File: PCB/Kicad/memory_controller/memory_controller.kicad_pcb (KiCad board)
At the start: 6 copper layers, 180 x 100 mm, 116 parts, among them U1 74245, U10 74283, U11 74377, U12 74377, U13 74245, U14 74245, U15 74245, U16 74245, U17 74245, U18 74245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

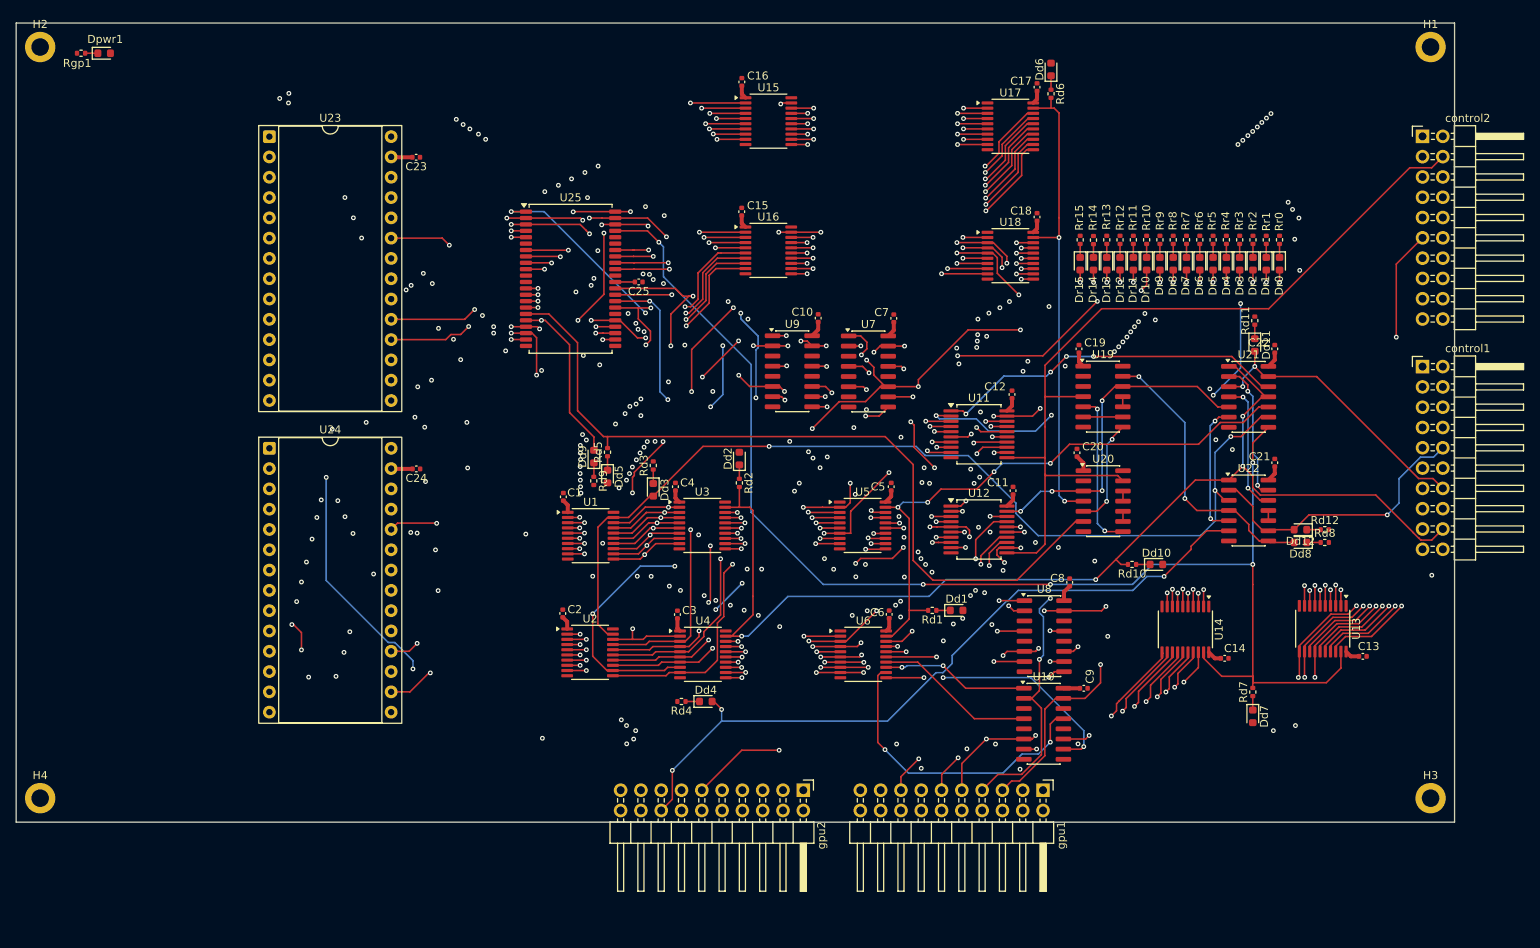
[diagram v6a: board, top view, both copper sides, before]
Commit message: drc ok, no silkscreen
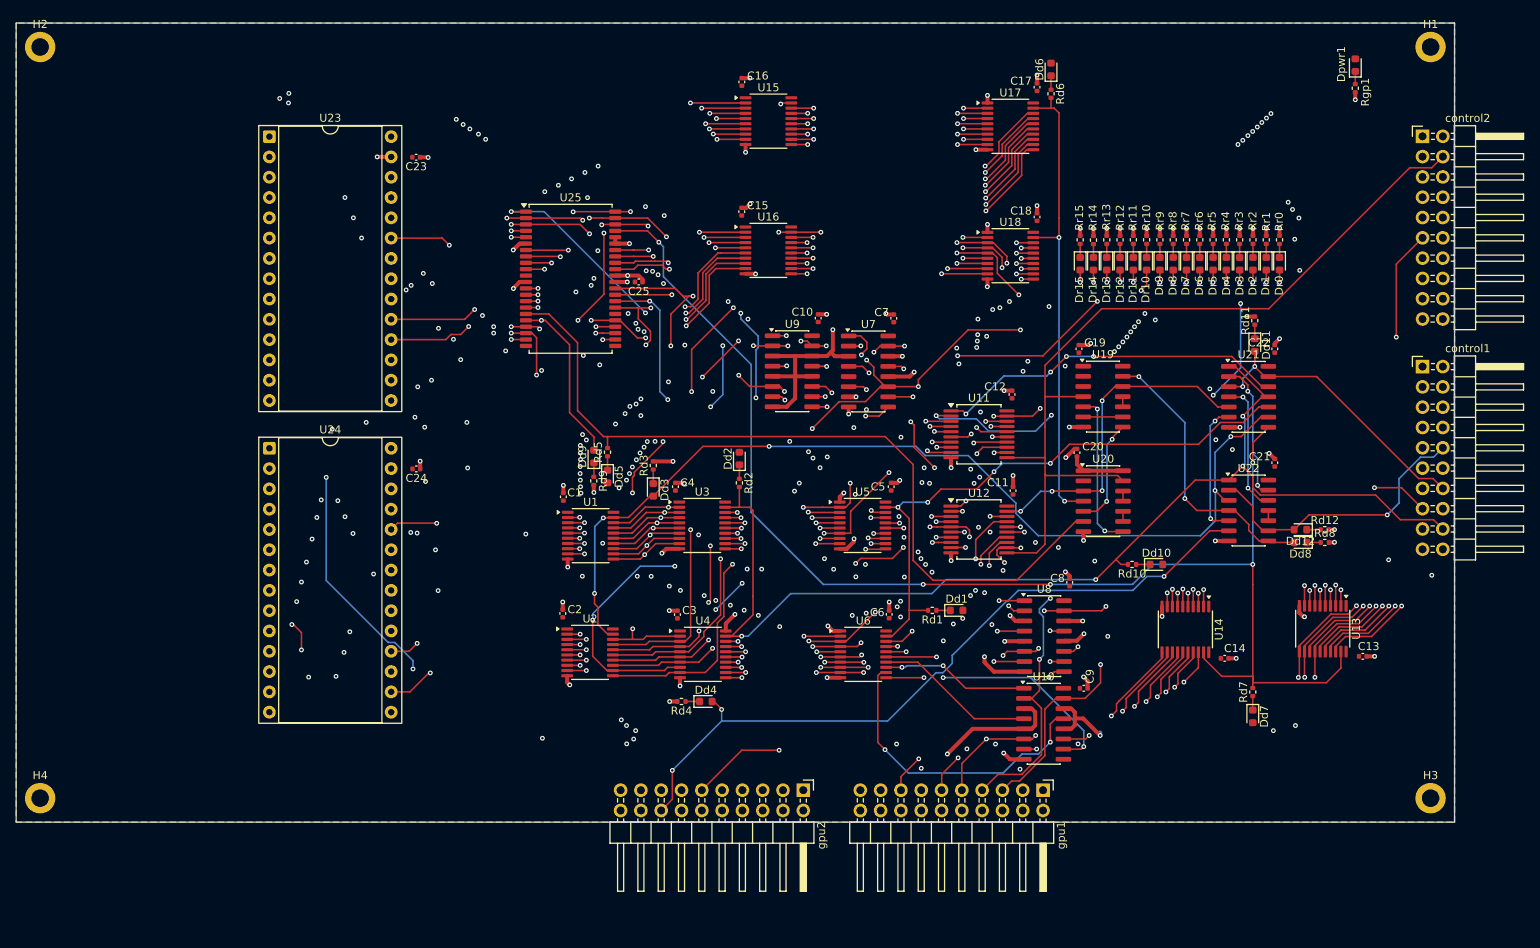
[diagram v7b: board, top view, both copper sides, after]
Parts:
- moved Rgp1 159.5 mm to (267.6, 78.2), turned to -90 degrees
- moved Dpwr1 156.6 mm to (267.6, 75.3), turned to 90 degrees
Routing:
- net GND: track 0.00 -> 169.1 mm, vias 0 -> 86
- net VCC: track 48.3 -> 13.0 mm, vias 0 -> 3
- net /DATA_BUS2: track 154.1 -> 136.6 mm, vias 2 -> 3
- net /DATA_BUS1: track 143.7 -> 137.1 mm, vias 2 -> 3
- net /~{OE}_n: track 146.3 -> 145.4 mm
- net /GPU_DATA6: track 198.0 -> 198.9 mm
- net /DATA_BUS0: track 134.8 -> 135.5 mm
- net /GPU_DATA5: track 192.8 -> 193.5 mm
- net /OUTPUT_ENABLE: track 121.5 -> 122.1 mm, vias 3 -> 5
- net /output_MUX/DATA_OUT1: track 128.4 -> 129.0 mm
- added copper zone on In1.Cu, net GND
- added copper zone on In4.Cu, net GND
- added copper zone on B.Cu, net VCC
- added copper zone on F.Cu, net VCC
- added copper zone on In2.Cu, net VCC
- added copper zone on In3.Cu, net VCC
